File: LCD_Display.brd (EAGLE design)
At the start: 41.9 x 30.5 mm, 4 parts, among them U1 NEWHAVEN_LCD

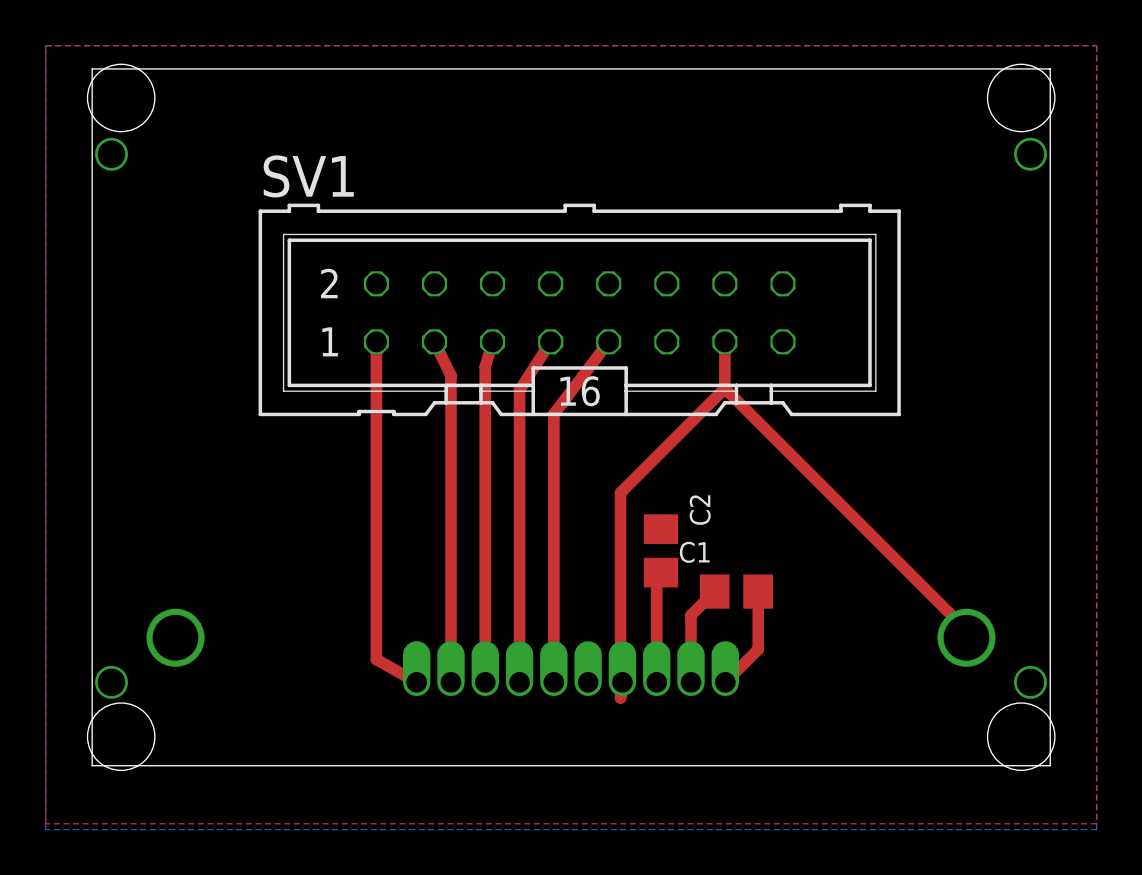
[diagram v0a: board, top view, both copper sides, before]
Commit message: Added dimensions, tidied up
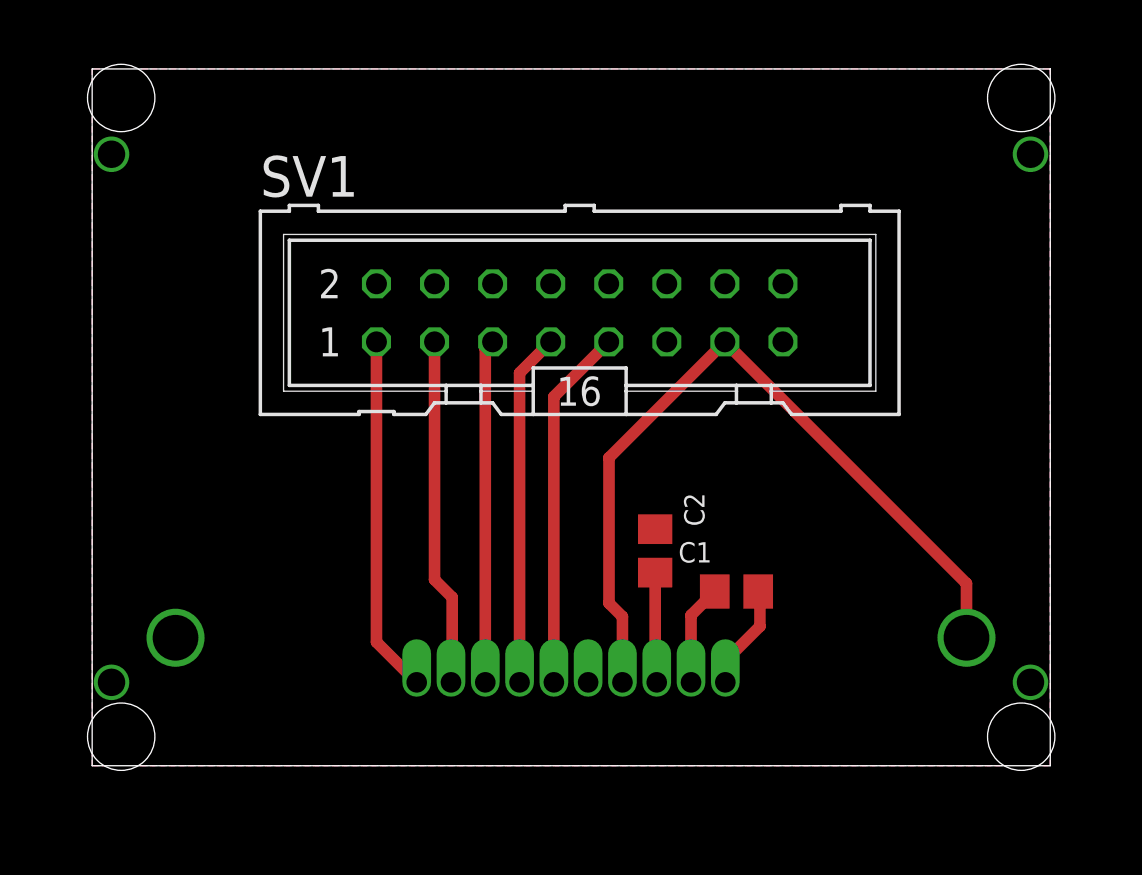
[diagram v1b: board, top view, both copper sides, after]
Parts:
- moved C2 0.25 mm to (24.6, 9.40)
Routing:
- net VDD: track 33.4 -> 34.6 mm
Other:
- board text added: "Sized for Eurocard unit"
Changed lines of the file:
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@@
 <setting verticaltext="up"/>
 </settings>
-<grid distance="0.05" unitdist="inch" unit="inch" style="lines" multiple="1" display="yes" altdistance="0.025" altunitdist="inch" altunit="inch"/>
+<grid distance="0.001" unitdist="inch" unit="inch" style="lines" multiple="1" display="yes" altdistance="0.025" altunitdist="inch" altunit="inch"/>
 <layers>
 <layer number="1" name="Top" color="4" fill="1" visible="yes" active="yes"/>
@@
 <hole x="40.64" y="29.21" drill="2.9464"/>
 <hole x="40.64" y="1.27" drill="2.9464"/>
+<dimension x1="0" y1="0" x2="41.91" y2="-2.54" x3="20.955" y3="-6.35" textsize="1.778" layer="48" dtype="horizontal" unit="inch" visible="yes"/>
+<dimension x1="0" y1="30.48" x2="-2.54" y2="0" x3="-2.2352" y3="15.24" textsize="1.778" layer="48" dtype="vertical" unit="inch" visible="yes"/>
+<dimension x1="1.27" y1="29.21" x2="40.64" y2="29.21" x3="20.955" y3="33.02" textsize="1.778" layer="48" dtype="horizontal" unit="inch" visible="yes"/>
+<dimension x1="40.64" y1="29.21" x2="40.64" y2="1.27" x3="49.53" y3="15.24" textsize="1.778" layer="48" dtype="vertical" unit="inch" visible="yes"/>
+<dimension x1="39.73554375" y1="30.372875" x2="41.54445625" y2="28.047125" x3="52.070009375" y3="38.0999875" textsize="1.778" layer="48" dtype="diameter" unit="inch" precision="3" visible="yes"/>
+<dimension x1="1.27" y1="29.21" x2="0.254" y2="27.3558" x3="-13.3858" y3="28.2829" textsize="1.778" layer="48" dtype="vertical" unit="inch"/>
+<wire x1="1.1176" y1="10.668" x2="0" y2="10.668" width="0.127" layer="48"/>
+<dimension x1="1.1176" y1="10.668" x2="0.254" y2="27.3558" x3="-13.3858" y3="19.0119" textsize="1.778" layer="48" dtype="vertical" unit="inch"/>
+<dimension x1="1.1176" y1="10.668" x2="40.7416" y2="10.6426" x3="20.9296" y3="-14.8844" textsize="1.778" layer="48" dtype="horizontal" unit="inch"/>
+<text x="-8.382" y="39.6748" size="1.778" layer="48">Sized for Eurocard unit</text>
 </plain>
 <attributes>
@@
 <param name="rvMicroViaOuter" value="0.25"/>
 <param name="rvMicroViaInner" value="0.25"/>
-<param name="rlMinPadTop" value="1mil"/>
+<param name="rlMinPadTop" value="7mil"/>
 <param name="rlMaxPadTop" value="20mil"/>
-<param name="rlMinPadInner" value="1mil"/>
+<param name="rlMinPadInner" value="7mil"/>
 <param name="rlMaxPadInner" value="20mil"/>
-<param name="rlMinPadBottom" value="1mil"/>
+<param name="rlMinPadBottom" value="7mil"/>
 <param name="rlMaxPadBottom" value="20mil"/>
 <param name="rlMinViaOuter" value="8mil"/>
@@
 <attribute name="PARTNO" value="1276-2396-1-ND" x="28.184" y="7.62" size="1.778" layer="27" display="off"/>
 </element>
-<element name="C2" library="rlc-jqi" package="0805" value="1uF" x="24.882" y="9.398" rot="R270">
-<attribute name="PARTNO" value="1276-2396-1-ND" x="24.882" y="9.398" size="1.778" layer="27" rot="R270" display="off"/>
+<element name="C2" library="rlc-jqi" package="0805" value="1uF" x="24.628" y="9.398" rot="R270">
+<attribute name="PARTNO" value="1276-2396-1-ND" x="24.628" y="9.398" size="1.778" layer="27" rot="R270" display="off"/>
 </element>
 </elements>
@@
 <contactref element="U1" pad="9"/>
 <contactref element="C1" pad="1"/>
-<wire x1="27.234" y1="7.62" x2="26.196" y2="6.582" width="0.508" layer="1"/>
-<wire x1="26.196" y1="6.582" x2="26.196" y2="3.648" width="0.508" layer="1"/>
+<wire x1="26.196" y1="3.648" x2="26.196" y2="6.582" width="0.508" layer="1"/>
+<wire x1="26.196" y1="6.582" x2="27.234" y2="7.62" width="0.508" layer="1"/>
 </signal>
 <signal name="N$2">
 <contactref element="C1" pad="2"/>
 <contactref element="U1" pad="10"/>
-<wire x1="27.696" y1="3.648" x2="29.134" y2="5.086" width="0.508" layer="1"/>
-<wire x1="29.134" y1="5.086" x2="29.134" y2="7.62" width="0.508" layer="1"/>
+<wire x1="27.696" y1="3.648" x2="27.696" y2="4.582" width="0.508" layer="1"/>
+<wire x1="27.696" y1="4.582" x2="29.21" y2="6.096" width="0.508" layer="1"/>
+<wire x1="29.21" y1="6.096" x2="29.21" y2="7.544" width="0.508" layer="1"/>
+<wire x1="29.21" y1="7.544" x2="29.134" y2="7.62" width="0.508" layer="1"/>
 </signal>
 <signal name="N$3">
 <contactref element="C2" pad="2"/>
 <contactref element="U1" pad="8"/>
-<wire x1="24.882" y1="8.448" x2="24.696" y2="8.262" width="0.508" layer="1"/>
-<wire x1="24.696" y1="8.262" x2="24.696" y2="3.648" width="0.508" layer="1"/>
+<wire x1="24.628" y1="8.448" x2="24.628" y2="3.716" width="0.508" layer="1"/>
+<wire x1="24.628" y1="3.716" x2="24.696" y2="3.648" width="0.508" layer="1"/>
 </signal>
 <signal name="GND">
@@
 <contactref element="U1" pad="K"/>
 <contactref element="SV1" pad="11"/>
-<polygon width="0.508" layer="1" isolate="0.254">
-<vertex x="-2.032" y="31.496"/>
-<vertex x="43.942" y="31.496"/>
-<vertex x="43.942" y="-2.54"/>
-<vertex x="-2.032" y="-2.54"/>
+<polygon width="0.508" layer="1" isolate="0.381">
+<vertex x="0" y="0"/>
+<vertex x="41.91" y="0"/>
+<vertex x="41.91" y="30.48"/>
+<vertex x="0" y="30.48"/>
 </polygon>
-<polygon width="0.508" layer="16">
-<vertex x="-2.032" y="31.496"/>
-<vertex x="43.942" y="31.496"/>
-<vertex x="43.942" y="-2.794"/>
-<vertex x="-2.032" y="-2.794"/>
+<polygon width="0.508" layer="16" isolate="0.381">
+<vertex x="0" y="30.48"/>
+<vertex x="41.91" y="30.48"/>
+<vertex x="41.91" y="0"/>
+<vertex x="0" y="0"/>
 </polygon>
 </signal>
@@
 <contactref element="U1" pad="7"/>
 <contactref element="SV1" pad="13"/>
-<wire x1="23.196" y1="3.648" x2="23.114" y2="2.968" width="0.508" layer="1"/>
-<wire x1="23.114" y1="2.968" x2="23.114" y2="11.938" width="0.508" layer="1"/>
-<wire x1="23.114" y1="11.938" x2="27.676" y2="16.5" width="0.508" layer="1"/>
-<wire x1="27.676" y1="16.5" x2="27.676" y2="18.542" width="0.508" layer="1"/>
-<wire x1="38.246" y1="5.598" x2="38.246" y2="5.93" width="0.508" layer="1"/>
-<wire x1="38.246" y1="5.93" x2="27.676" y2="16.5" width="0.508" layer="1"/>
+<wire x1="22.606" y1="13.472" x2="27.676" y2="18.542" width="0.508" layer="1"/>
+<wire x1="23.196" y1="3.648" x2="23.196" y2="6.522" width="0.508" layer="1"/>
+<wire x1="23.196" y1="6.522" x2="22.606" y2="7.112" width="0.508" layer="1"/>
+<wire x1="22.606" y1="7.112" x2="22.606" y2="13.472" width="0.508" layer="1"/>
+<wire x1="38.246" y1="5.598" x2="38.246" y2="7.972" width="0.508" layer="1"/>
+<wire x1="38.246" y1="7.972" x2="27.676" y2="18.542" width="0.508" layer="1"/>
 </signal>
 <signal name="SI">
 <contactref element="U1" pad="5"/>
 <contactref element="SV1" pad="9"/>
-<wire x1="22.596" y1="18.542" x2="20.196" y2="15.38" width="0.508" layer="1"/>
-<wire x1="20.196" y1="15.38" x2="20.196" y2="3.648" width="0.508" layer="1"/>
+<wire x1="20.196" y1="3.648" x2="20.196" y2="16.142" width="0.508" layer="1"/>
+<wire x1="20.196" y1="16.142" x2="22.596" y2="18.542" width="0.508" layer="1"/>
 </signal>
 <signal name="SCL">
 <contactref element="U1" pad="4"/>
 <contactref element="SV1" pad="7"/>
-<wire x1="20.056" y1="18.542" x2="18.696" y2="16.42" width="0.508" layer="1"/>
-<wire x1="18.696" y1="16.42" x2="18.696" y2="3.648" width="0.508" layer="1"/>
+<wire x1="18.696" y1="3.648" x2="18.696" y2="17.182" width="0.508" layer="1"/>
+<wire x1="18.696" y1="17.182" x2="20.056" y2="18.542" width="0.508" layer="1"/>
 </signal>
 <signal name="CSB">
 <contactref element="U1" pad="3"/>
 <contactref element="SV1" pad="5"/>
-<wire x1="17.516" y1="18.542" x2="17.196" y2="17.46" width="0.508" layer="1"/>
-<wire x1="17.196" y1="17.46" x2="17.196" y2="3.648" width="0.508" layer="1"/>
+<wire x1="17.196" y1="3.648" x2="17.196" y2="18.222" width="0.508" layer="1"/>
+<wire x1="17.196" y1="18.222" x2="17.516" y2="18.542" width="0.508" layer="1"/>
 </signal>
 <signal name="RS">
 <contactref element="U1" pad="2"/>
 <contactref element="SV1" pad="3"/>
-<wire x1="14.976" y1="18.542" x2="15.696" y2="17.06" width="0.508" layer="1"/>
-<wire x1="15.696" y1="17.06" x2="15.696" y2="3.648" width="0.508" layer="1"/>
+<wire x1="14.976" y1="18.542" x2="14.976" y2="8.138" width="0.508" layer="1"/>
+<wire x1="14.976" y1="8.138" x2="15.748" y2="7.366" width="0.508" layer="1"/>
+<wire x1="15.748" y1="7.366" x2="15.748" y2="3.7" width="0.508" layer="1"/>
+<wire x1="15.748" y1="3.7" x2="15.696" y2="3.648" width="0.508" layer="1"/>
 </signal>
 <signal name="RST">
 <contactref element="U1" pad="1"/>
 <contactref element="SV1" pad="1"/>
-<wire x1="14.196" y1="3.648" x2="12.436" y2="4.646" width="0.508" layer="1"/>
-<wire x1="12.436" y1="4.646" x2="12.436" y2="18.542" width="0.508" layer="1"/>
+<wire x1="12.436" y1="18.542" x2="12.436" y2="5.408" width="0.508" layer="1"/>
+<wire x1="12.436" y1="5.408" x2="14.196" y2="3.648" width="0.508" layer="1"/>
 </signal>
 </signals>
